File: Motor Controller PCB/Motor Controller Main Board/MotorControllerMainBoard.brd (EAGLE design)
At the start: 99 x 100 mm, 94 parts, among them T1 TEENSY_3.1_ALL_PINS

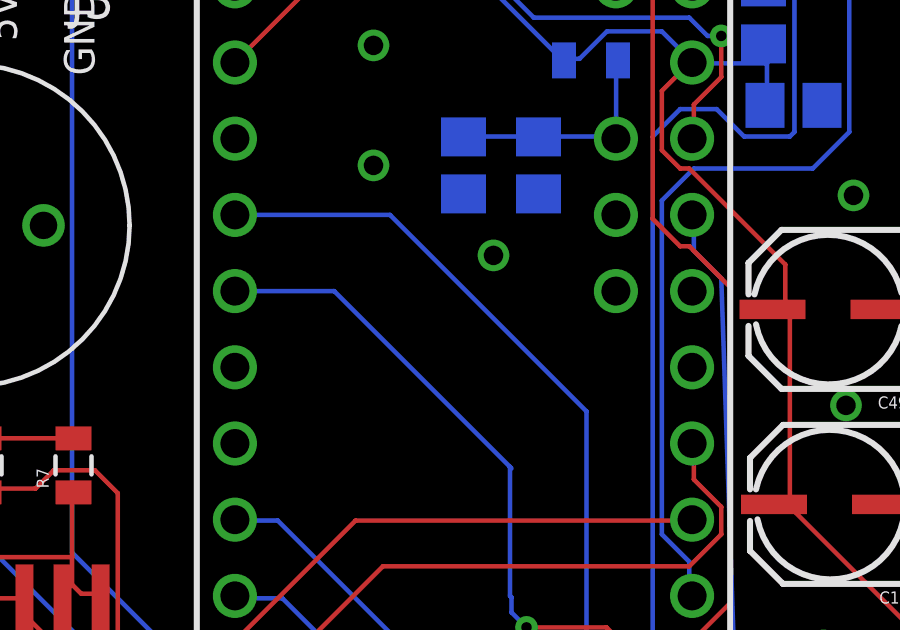
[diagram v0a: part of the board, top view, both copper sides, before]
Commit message: Added pull down resistors
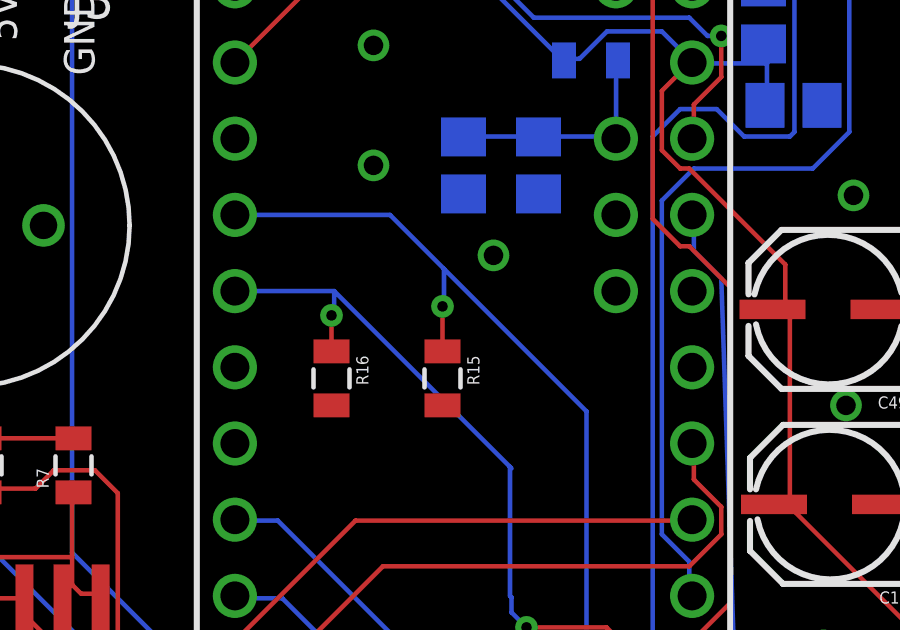
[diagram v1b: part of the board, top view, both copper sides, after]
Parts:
- added R15, R16: 10k, SparkFun-Passives:0805
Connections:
- net BUTTON1: now also R15.1
- net BUTTON2: now also R16.1
- net GND: now also R15.2, R16.2
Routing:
- net BUTTON1: track 42.2 -> 45.0 mm, vias 1 -> 2
- net BUTTON2: track 40.0 -> 42.0 mm, vias 2 -> 3
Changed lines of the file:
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@@
 <element name="J2" library="SparkFun-Connectors" package="2X4" value="" x="95" y="43" rot="R90"/>
 <element name="J3" library="SparkFun-Connectors" package="1X03" value="" x="70" y="84" rot="R180"/>
+<element name="R15" library="SparkFun-Passives" package="0805" value="10k" x="82.3" y="68.9" rot="R270"/>
+<element name="R16" library="SparkFun-Passives" package="0805" value="10k" x="78.6" y="68.9" rot="R270"/>
 </elements>
 <signals>
@@
 <via x="7" y="88" extent="1-16" drill="0.65"/>
 <via x="12" y="96" extent="1-16" drill="0.65"/>
+<contactref element="R15" pad="2"/>
+<contactref element="R16" pad="2"/>
 <wire x1="61" y1="95" x2="60" y2="96.75" width="0" layer="19" extent="1-1"/>
 <wire x1="78.8" y1="37.75" x2="79.05" y2="41" width="0" layer="19" extent="1-1"/>
@@
 <contactref element="T1" pad="3"/>
 <wire x1="75.38" y1="74.35" x2="80.55" y2="74.35" width="0.1524" layer="16"/>
-<wire x1="80.55" y1="74.35" x2="87.1" y2="67.8" width="0.1524" layer="16"/>
+<wire x1="80.55" y1="74.35" x2="82.35" y2="72.55" width="0.1524" layer="16"/>
+<wire x1="82.35" y1="72.55" x2="87.1" y2="67.8" width="0.1524" layer="16"/>
 <wire x1="90.2202" y1="53.0648" x2="90.3352" y2="53.0648" width="0.1524" layer="16"/>
 <wire x1="90.3352" y1="53.0648" x2="90.8" y2="52.6" width="0.1524" layer="16"/>
@@
 <wire x1="94.9" y1="48.8" x2="94.9" y2="45.64" width="0.1524" layer="1"/>
 <wire x1="94.9" y1="45.64" x2="96.27" y2="44.27" width="0.1524" layer="1"/>
+<contactref element="R15" pad="1"/>
+<wire x1="82.35" y1="72.55" x2="82.35" y2="71.35" width="0.1524" layer="16"/>
+<wire x1="82.35" y1="71.35" x2="82.3" y2="71.3" width="0.1524" layer="16"/>
+<via x="82.3" y="71.3" extent="1-16" drill="0.35"/>
+<wire x1="82.3" y1="71.3" x2="82.3" y2="69.8" width="0.1524" layer="1"/>
 </signal>
 <signal name="BUTTON2">
@@
 <wire x1="96.2" y1="56.8" x2="96.2" y2="46.88" width="0.1524" layer="16"/>
 <wire x1="96.2" y1="46.88" x2="96.27" y2="46.81" width="0.1524" layer="16"/>
+<contactref element="R16" pad="1"/>
+<wire x1="78.69" y1="71.81" x2="78.69" y2="71.09" width="0.1524" layer="16"/>
+<wire x1="78.69" y1="71.09" x2="78.6" y2="71" width="0.1524" layer="16"/>
+<via x="78.6" y="71" extent="1-16" drill="0.35"/>
+<wire x1="78.6" y1="71" x2="78.6" y2="69.8" width="0.1524" layer="1"/>
 </signal>
 <signal name="HALL">

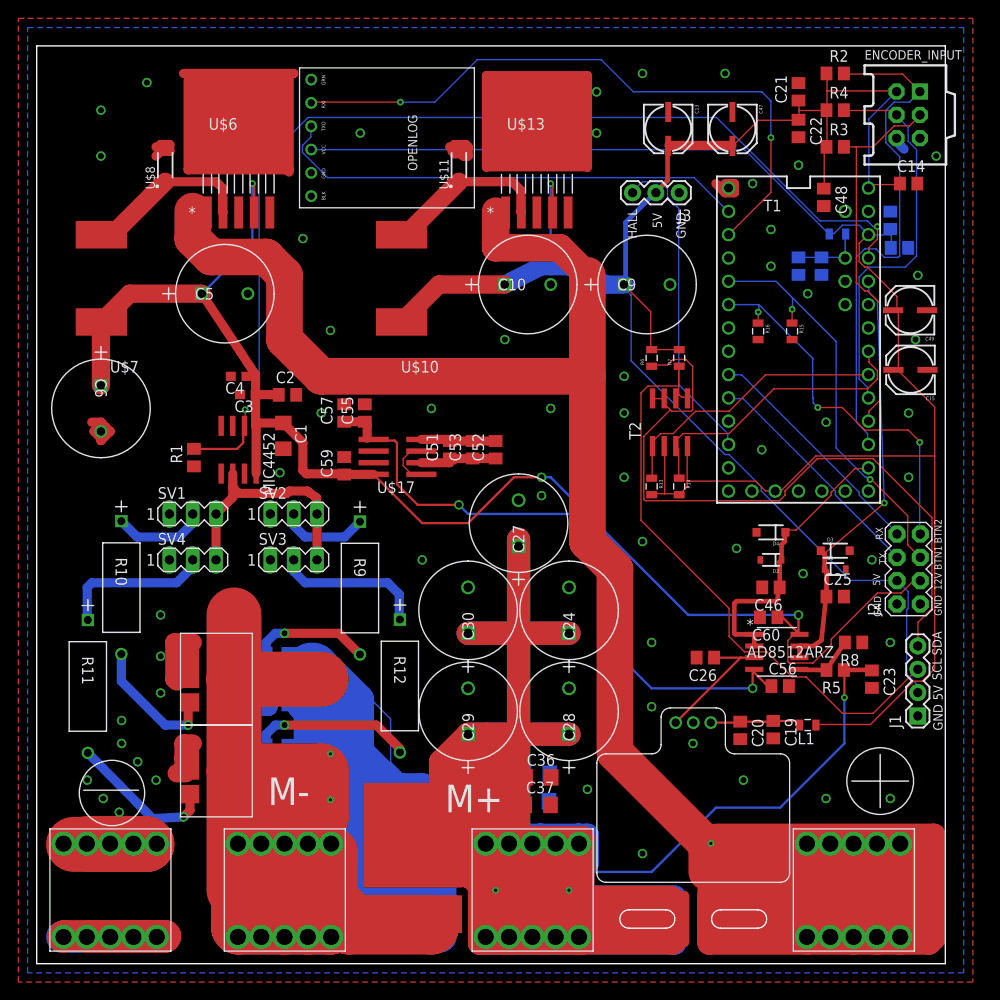
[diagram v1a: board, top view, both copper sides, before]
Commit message: Added labels on FET jumpers + minor tweaks to traces
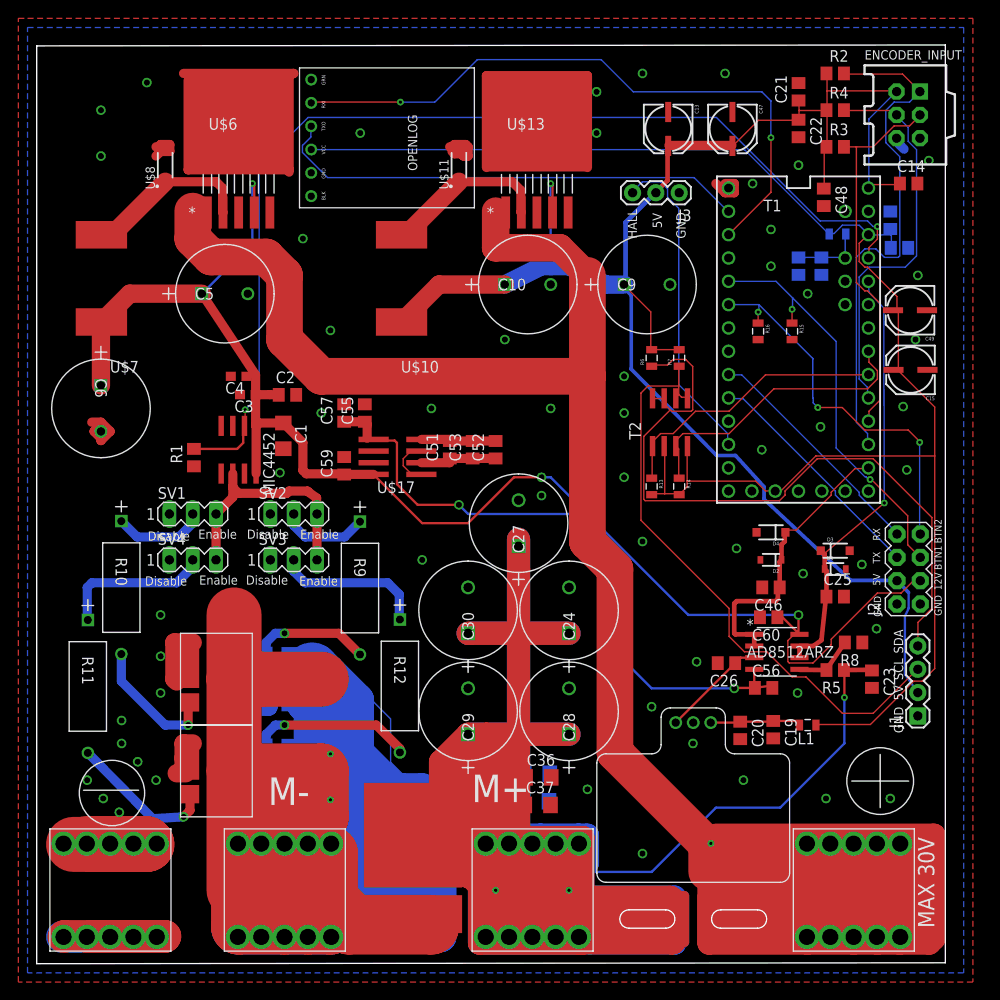
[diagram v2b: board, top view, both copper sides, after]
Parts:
- moved C26 2.38 mm to (75.2, 32.8)
- moved C56 1.81 mm to (79.2, 30.1)
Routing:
- net CURRENT_SENSOR_OUTPUT: track 14.4 -> 11.5 mm
- net 5V_POWER_REGULATED: track 185.0 -> 186.0 mm
- net OUTPUT_12NEG: track 70.8 -> 69.9 mm
- net GND: vias 55 -> 56
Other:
- board size 99 x 100 mm -> 99 x 100.1 mm
- board text added: "Disable"
- board text added: "Enable"
- board text added: "MAX 30V"
